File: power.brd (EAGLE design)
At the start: 27.6 x 17.8 mm, 12 parts, among them IC1 UC27775, J2 USB-MINIB-TH-VERTICAL-5PIN, U1 MCP73831, U2 Tiny85-20-SMT, X1 Micro USB

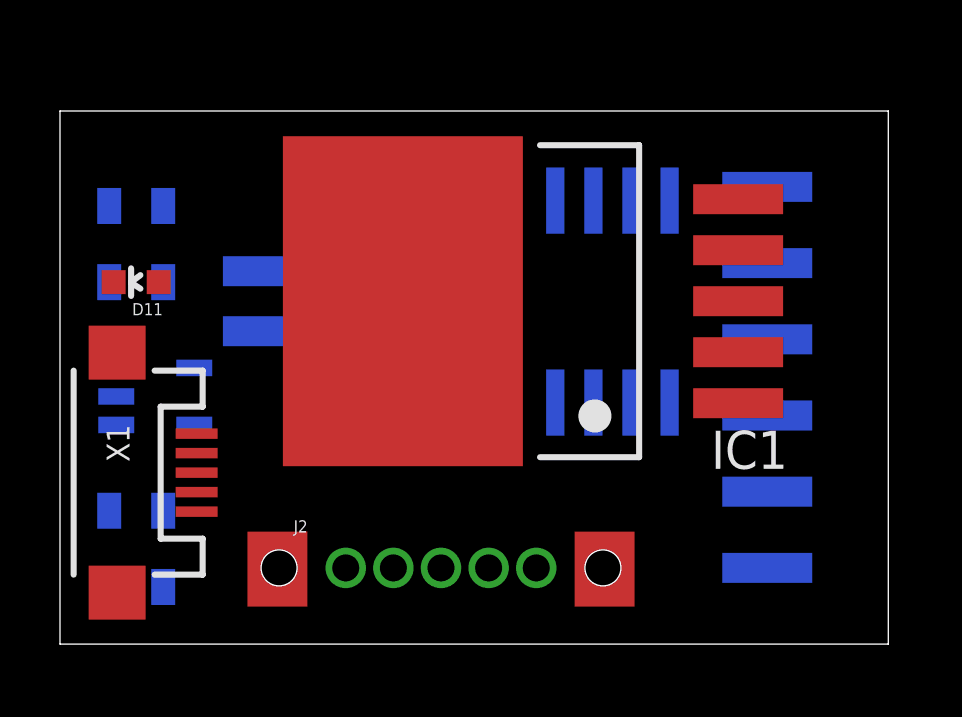
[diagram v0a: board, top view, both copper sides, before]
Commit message: Got a good handle on the bt module so went ahead and ordered one
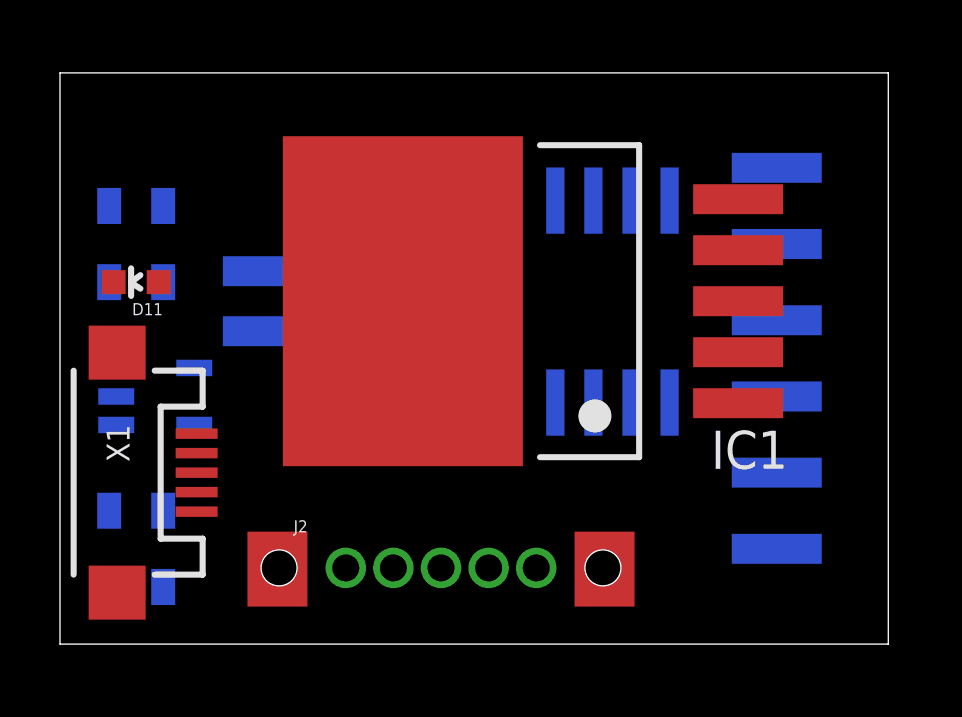
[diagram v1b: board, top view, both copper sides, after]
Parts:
- moved JP1 0.71 mm to (28.9, 9.53)
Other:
- board size 27.6 x 17.8 mm -> 27.6 x 19 mm
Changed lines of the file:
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@@
 <plain>
 <wire x1="0" y1="0" x2="27.61" y2="0" width="0" layer="20"/>
-<wire x1="27.61" y1="0" x2="27.61" y2="17.77" width="0" layer="20"/>
-<wire x1="27.61" y1="17.77" x2="0" y2="17.77" width="0" layer="20"/>
-<wire x1="0" y1="17.77" x2="0" y2="0" width="0" layer="20"/>
+<wire x1="27.61" y1="0" x2="27.61" y2="19.04" width="0" layer="20"/>
+<wire x1="27.61" y1="19.04" x2="0" y2="19.04" width="0" layer="20"/>
+<wire x1="0" y1="19.04" x2="0" y2="0" width="0" layer="20"/>
 <text x="8.89" y="23.495" size="1.778" layer="51">400mAh LiPo</text>
-<rectangle x1="29.845" y1="0" x2="59.055" y2="17.78" layer="52"/>
+<rectangle x1="29.845" y1="0" x2="59.3725" y2="19.05" layer="52"/>
 <text x="50.165" y="9.8425" size="1.016" layer="51" rot="R180">RN42-HID Module</text>
 <dimension x1="50.8" y1="0" x2="50.8" y2="33.5" x3="52.07" y3="16.75" textsize="1.016" layer="51"/>
@@
 <attribute name="PROD_ID" value="IC-09092" x="18.415" y="11.43" size="1.778" layer="28" rot="MR0" display="off"/>
 </element>
-<element name="JP1" library="mine" package="1X06-SMD-NOHOLES" value="RA 6Pin SMD" x="28.575" y="8.89" smashed="yes" rot="MR270">
-<attribute name="PROD_ID" value="CONN-08971" x="28.575" y="8.89" size="1.778" layer="28" rot="MR270" display="off"/>
-<attribute name="NAME" x="26.67" y="10.795" size="0.8128" layer="26" rot="MR270"/>
+<element name="JP1" library="mine" package="1X06-SMD-NOHOLES" value="RA 6Pin SMD" x="28.8925" y="9.525" smashed="yes" rot="MR270">
+<attribute name="PROD_ID" value="CONN-08971" x="28.8925" y="9.525" size="1.778" layer="28" rot="MR270" display="off"/>
+<attribute name="NAME" x="26.9875" y="11.43" size="0.8128" layer="26" rot="MR270"/>
 </element>
 <element name="IC1" library="mine" package="TO263_5" value="UC27775" x="14.605" y="11.43" rot="R90">
@@
 <contactref element="JP1" pad="6"/>
 <contactref element="IC1" pad="5"/>
-<wire x1="23.575" y1="2.54" x2="22.605" y2="14.83" width="0" layer="19" extent="1-16"/>
+<wire x1="23.8925" y1="3.175" x2="22.605" y2="14.83" width="0" layer="19" extent="1-16"/>
 <wire x1="7.73" y1="12.43" x2="22.605" y2="14.83" width="0" layer="19" extent="1-16"/>
 <wire x1="3.44" y1="14.605" x2="7.73" y2="12.43" width="0" layer="19" extent="16-16"/>
@@
 <contactref element="IC1" pad="3"/>
 <contactref element="J2" pad="GND"/>
-<wire x1="22.605" y1="11.43" x2="23.575" y2="15.24" width="0" layer="19" extent="1-16"/>
+<wire x1="22.605" y1="11.43" x2="23.8925" y2="15.875" width="0" layer="19" extent="1-16"/>
 <wire x1="7.73" y1="10.43" x2="22.605" y2="11.43" width="0" layer="19" extent="1-16"/>
 <wire x1="1.8749" y1="8.255" x2="7.73" y2="10.43" width="0" layer="19" extent="16-16"/>
@@
 <contactref element="JP1" pad="4"/>
 <contactref element="J2" pad="D-"/>
-<wire x1="11.1125" y1="2.54" x2="23.575" y2="7.62" width="0" layer="19" extent="16-16"/>
+<wire x1="11.1125" y1="2.54" x2="23.8925" y2="8.255" width="0" layer="19" extent="16-16"/>
 </signal>
 <signal name="N$3">
 <contactref element="JP1" pad="3"/>
 <contactref element="J2" pad="D+"/>
-<wire x1="12.7" y1="2.54" x2="23.575" y2="10.16" width="0" layer="19" extent="16-16"/>
+<wire x1="12.7" y1="2.54" x2="23.8925" y2="10.795" width="0" layer="19" extent="16-16"/>
 </signal>
 <signal name="VCC">
@@
 <contactref element="JP1" pad="5"/>
 <contactref element="J2" pad="VBUS"/>
-<wire x1="23.575" y1="5.08" x2="22.605" y2="13.13" width="0" layer="19" extent="1-16"/>
-<wire x1="9.525" y1="2.54" x2="23.575" y2="5.08" width="0" layer="19" extent="16-16"/>
+<wire x1="23.8925" y1="5.715" x2="22.605" y2="13.13" width="0" layer="19" extent="1-16"/>
+<wire x1="9.525" y1="2.54" x2="23.8925" y2="5.715" width="0" layer="19" extent="16-16"/>
 </signal>
 </signals>

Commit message: Added a switch and playing around with the arrangement
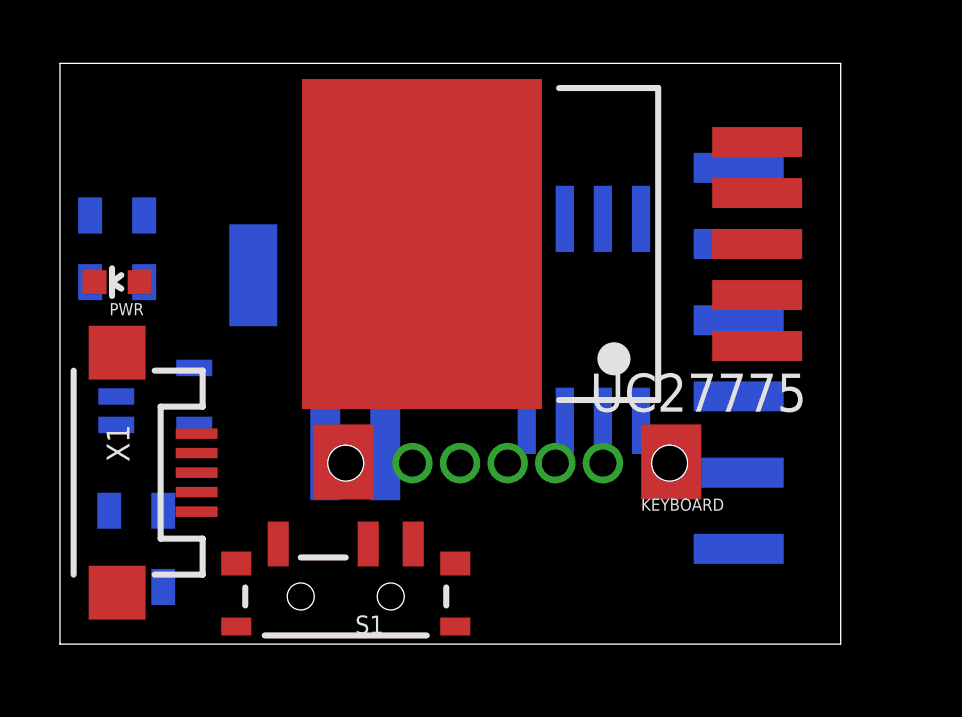
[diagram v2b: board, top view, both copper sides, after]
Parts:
- removed D11: RED, SparkFun:LED-0603
- removed IC1: UC27775, mine:TO263_5
- removed J2: USB-MINIB-TH-VERTICAL-5PIN, mine:USB-MINIB-TH-VERTICAL
- removed JP1: RA 6Pin SMD, mine:1X06-SMD-NOHOLES
- removed JP7: LiPo Battery, SparkFun:JST-2-SMD
- added BAT: LiPo Battery, SparkFun:JST-2-SMD
- added BT: RA 6Pin SMD, mine:1X06-SMD-NOHOLES
- added KEYBOARD: USB-MINIB-TH-VERTICAL-5PIN, mine:USB-MINIB-TH-VERTICAL
- added PWR: RED, SparkFun:LED-0603
- added S1: (no value), SparkFun-Electromechanical:SWITCH-SPST-SMD-A
- added UC27775: UC27775, mine:TO263_5
- moved U2 1.14 mm to (17.5, 10.8), turned to 180 degrees
- moved C2 0.71 mm to (1.91, 14.3)
- moved R1 0.64 mm to (1.91, 12.1), turned to 180 degrees
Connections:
- new net VBAT2: BAT.2, C2.1, S1.1, U1.3
- net GND: now also BAT.1, BT.1, KEYBOARD.GND, UC27775.3; no longer IC1.3, J2.GND, JP1.1, JP7.1
- net N$12: now also PWR.A; no longer D11.A
- net N$2: now also BT.4, KEYBOARD.D-; no longer J2.D-, JP1.4
- net N$3: now also BT.3, KEYBOARD.D+; no longer J2.D+, JP1.3
- net STAT: now also PWR.C; no longer D11.C
- net VBAT: now also BT.6, S1.3, UC27775.5; no longer C2.1, IC1.5, JP1.6, JP7.2, U1.3
- net VCC: now also BT.5, KEYBOARD.VBUS, UC27775.4; no longer IC1.4, J2.VBUS, JP1.5
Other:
- board size 27.6 x 19 mm -> 26 x 19.4 mm

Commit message: Using mini usb instead of micro
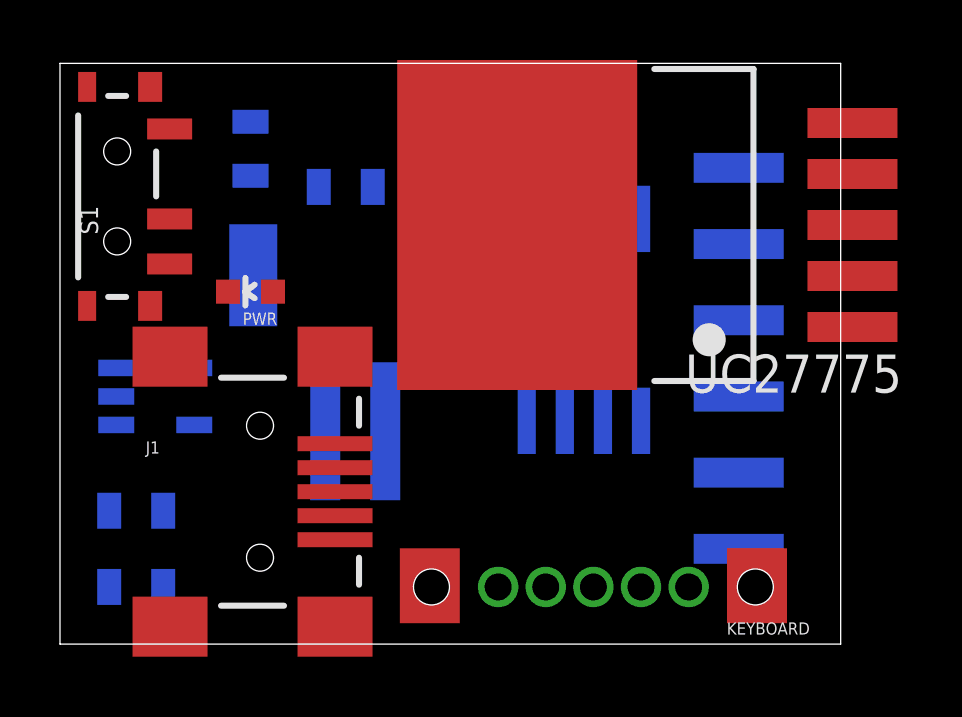
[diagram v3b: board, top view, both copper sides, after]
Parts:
- removed X1: Micro USB, SparkFun:USB-MICROB
- added J1: USB-MINIB-5PIN, SparkFun-Connectors:USB-MINIB
- moved S1 15.4 mm to (1.91, 14.9), turned to 90 degrees
- moved R1 8.25 mm to (9.53, 15.2)
- moved KEYBOARD 5.02 mm to (17.8, 1.91)
- moved C2 4.97 mm to (6.35, 16.5), turned to 270 degrees
- moved PWR 4.46 mm to (6.35, 11.7)
- moved UC27775 3.24 mm to (18.4, 14.0)
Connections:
- net GND: now also J1.GND; no longer X1.GND
- net VIN: now also J1.VBUS; no longer X1.VBUS
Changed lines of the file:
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@@
 <?xml version="1.0" encoding="utf-8"?>
 <!DOCTYPE eagle SYSTEM "eagle.dtd">
-<eagle version="6.6.0">
+<eagle version="7.4.0">
 <drawing>
 <settings>
@@
 <pass name="Default">
 <param name="RoutingGrid" value="50mil"/>
+<param name="AutoGrid" value="1"/>
+<param name="Efforts" value="0"/>
+<param name="TopRouterVariant" value="1"/>
 <param name="tpViaShape" value="round"/>
 <param name="PrefDir.1" value="|"/>
@@
 </autorouter>
 <elements>
-<element name="R1" library="SparkFun-Resistors" package="0805" value="330" x="1.905" y="12.065" rot="MR180">
-<attribute name="PROD_ID" value="RES-09883" x="1.905" y="12.065" size="1.778" layer="28" rot="MR180" display="off"/>
-</element>
-<element name="PWR" library="SparkFun" package="LED-0603" value="RED" x="1.905" y="12.065" rot="R90"/>
+<element name="R1" library="SparkFun-Resistors" package="0805" value="330" x="9.525" y="15.24" rot="MR180">
+<attribute name="PROD_ID" value="RES-09883" x="9.525" y="15.24" size="1.778" layer="28" rot="MR180" display="off"/>
+</element>
+<element name="PWR" library="SparkFun" package="LED-0603" value="RED" x="6.35" y="11.7475" rot="R90"/>
 <element name="U1" library="SparkFun" package="SOT23-5" value="MCP73831" x="3.175" y="8.255" rot="MR90"/>
 <element name="BAT" library="SparkFun" package="JST-2-SMD" value="LiPo Battery" x="9.8425" y="10.795" smashed="yes" rot="MR0">
@@
 <attribute name="VALUE" x="11.1125" y="10.795" size="0.4064" layer="28" rot="MR0"/>
 </element>
-<element name="X1" library="SparkFun" package="USB-MICROB" value="Micro USB" x="1.905" y="5.715" rot="R270"/>
 <element name="R2" library="SparkFun-Resistors" package="0805" value="2k" x="2.54" y="4.445" rot="MR180">
 <attribute name="PROD_ID" value="RES-09883" x="2.54" y="4.445" size="1.778" layer="28" rot="MR180" display="off"/>
@@
 <attribute name="PROD_ID" value="CAP-11625" x="2.54" y="1.905" size="1.778" layer="28" rot="MR0" display="off"/>
 </element>
-<element name="C2" library="SparkFun-Capacitors" package="0805-CAP" value="4.7uF" x="1.905" y="14.2875" rot="MR0">
-<attribute name="PROD_ID" value="CAP-11625" x="1.905" y="14.2875" size="1.778" layer="28" rot="MR0" display="off"/>
+<element name="C2" library="SparkFun-Capacitors" package="0805-CAP" value="4.7uF" x="6.35" y="16.51" rot="MR270">
+<attribute name="PROD_ID" value="CAP-11625" x="6.35" y="16.51" size="1.778" layer="28" rot="MR270" display="off"/>
 </element>
 <element name="U2" library="SparkFun-DigitalIC" package="SO08-EIAJ" value="Tiny85-20-SMT" x="17.4625" y="10.795" rot="MR180">
@@
 <attribute name="NAME" x="25.7175" y="11.43" size="0.8128" layer="26" rot="MR270"/>
 </element>
-<element name="UC27775" library="mine" package="TO263_5" value="UC27775" x="15.24" y="13.335" rot="R90">
-<attribute name="MF" value="TI" x="15.24" y="13.335" size="1.778" layer="27" rot="R90" display="off"/>
-</element>
-<element name="KEYBOARD" library="mine" package="USB-MINIB-TH-VERTICAL" value="USB-MINIB-TH-VERTICAL-5PIN" x="14.9225" y="6.0325" rot="R180">
-<attribute name="PROD_ID" value="CONN-08193" x="14.9225" y="6.0325" size="1.016" layer="27" rot="R180" display="off"/>
-</element>
-<element name="S1" library="SparkFun-Electromechanical" package="SWITCH-SPST-SMD-A" value="" x="9.525" y="1.5875" rot="R180"/>
+<element name="UC27775" library="mine" package="TO263_5" value="UC27775" x="18.415" y="13.97" rot="R90">
+<attribute name="MF" value="TI" x="18.415" y="13.97" size="1.778" layer="27" rot="R90" display="off"/>
+</element>
+<element name="KEYBOARD" library="mine" package="USB-MINIB-TH-VERTICAL" value="USB-MINIB-TH-VERTICAL-5PIN" x="17.78" y="1.905" rot="R180">
+<attribute name="PROD_ID" value="CONN-08193" x="17.78" y="1.905" size="1.016" layer="27" rot="R180" display="off"/>
+</element>
+<element name="S1" library="SparkFun-Electromechanical" package="SWITCH-SPST-SMD-A" value="" x="1.905" y="14.9225" rot="R90"/>
+<element name="J1" library="SparkFun-Connectors" package="USB-MINIB" value="USB-MINIB-5PIN" x="6.6675" y="5.08">
+<attribute name="PROD_ID" value="CONN-08193" x="6.6675" y="5.08" size="1.778" layer="27" display="off"/>
+</element>
 </elements>
 <signals>
@@
 <contactref element="UC27775" pad="5"/>
 <contactref element="S1" pad="3"/>
-<wire x1="22.6225" y1="3.175" x2="23.24" y2="16.735" width="0" layer="19" extent="1-16"/>
-<wire x1="7.275" y1="3.3375" x2="23.24" y2="16.735" width="0" layer="19" extent="1-1"/>
+<wire x1="22.6225" y1="3.175" x2="26.415" y2="17.37" width="0" layer="19" extent="1-16"/>
+<wire x1="3.655" y1="17.1725" x2="26.415" y2="17.37" width="0" layer="19" extent="1-1"/>
 </signal>
 <signal name="VIN">
 <contactref element="U1" pad="4"/>
-<contactref element="X1" pad="VBUS"/>
 <contactref element="C1" pad="1"/>
 <contactref element="R1" pad="1"/>
-<wire x1="4.4751" y1="9.205" x2="1.005" y2="12.065" width="0" layer="19" extent="16-16"/>
-<wire x1="4.555" y1="7.015" x2="4.4751" y2="9.205" width="0" layer="19" extent="1-16"/>
-<wire x1="3.44" y1="1.905" x2="4.555" y2="7.015" width="0" layer="19" extent="1-16"/>
+<contactref element="J1" pad="VBUS"/>
+<wire x1="8.625" y1="15.24" x2="4.4751" y2="9.205" width="0" layer="19" extent="16-16"/>
+<wire x1="9.1675" y1="6.68" x2="8.625" y2="15.24" width="0" layer="19" extent="1-16"/>
+<wire x1="3.44" y1="1.905" x2="4.4751" y2="9.205" width="0" layer="19" extent="16-16"/>
 </signal>
 <signal name="GND">
-<contactref element="X1" pad="GND"/>
 <contactref element="R2" pad="1"/>
 <contactref element="BT" pad="1"/>
@@
 <contactref element="C2" pad="2"/>
 <contactref element="BAT" pad="1"/>
-<wire x1="23.24" y1="13.335" x2="22.6225" y2="15.875" width="0" layer="19" extent="1-16"/>
-<wire x1="10.8425" y1="7.095" x2="23.24" y2="13.335" width="0" layer="19" extent="1-16"/>
-<wire x1="11.7475" y1="6.0325" x2="10.8425" y2="7.095" width="0" layer="19" extent="16-16"/>
-<wire x1="4.555" y1="4.415" x2="10.8425" y2="7.095" width="0" layer="19" extent="1-16"/>
-<wire x1="1.64" y1="4.445" x2="4.555" y2="4.415" width="0" layer="19" extent="1-16"/>
+<contactref element="J1" pad="GND"/>
+<wire x1="26.415" y1="13.97" x2="22.6225" y2="15.875" width="0" layer="19" extent="1-16"/>
+<wire x1="14.605" y1="1.905" x2="26.415" y2="13.97" width="0" layer="19" extent="1-1"/>
+<wire x1="10.8425" y1="7.095" x2="14.605" y2="1.905" width="0" layer="19" extent="16-16"/>
+<wire x1="1.8749" y1="8.255" x2="10.8425" y2="7.095" width="0" layer="19" extent="16-16"/>
+<wire x1="1.64" y1="4.445" x2="1.8749" y2="8.255" width="0" layer="19" extent="16-16"/>
 <wire x1="1.64" y1="1.905" x2="1.64" y2="4.445" width="0" layer="19" extent="16-16"/>
-<wire x1="1.8749" y1="8.255" x2="1.64" y2="4.445" width="0" layer="19" extent="16-16"/>
-<wire x1="1.005" y1="14.2875" x2="1.8749" y2="8.255" width="0" layer="19" extent="16-16"/>
+<wire x1="9.1675" y1="3.48" x2="1.64" y2="1.905" width="0" layer="19" extent="1-16"/>
+<wire x1="6.35" y1="15.61" x2="1.8749" y2="8.255" width="0" layer="19" extent="16-16"/>
 </signal>
 <signal name="N$12">
 <contactref element="PWR" pad="A"/>
 <contactref element="R1" pad="2"/>
-<wire x1="2.655" y1="12.065" x2="2.805" y2="12.065" width="0" layer="19" extent="1-16"/>
+<wire x1="7.1" y1="11.7475" x2="10.425" y2="15.24" width="0" layer="19" extent="1-16"/>
 </signal>
 <signal name="PROG">
@@
 <contactref element="PWR" pad="C"/>
 <contactref element="U1" pad="1"/>
-<wire x1="1.8749" y1="7.305" x2="1.155" y2="12.065" width="0" layer="19" extent="1-16"/>
+<wire x1="1.8749" y1="7.305" x2="5.6" y2="11.7475" width="0" layer="19" extent="1-16"/>
 </signal>
 <signal name="N$2">
 <contactref element="BT" pad="4"/>
 <contactref element="KEYBOARD" pad="D-"/>
-<wire x1="16.51" y1="6.0325" x2="22.6225" y2="8.255" width="0" layer="19" extent="16-16"/>
+<wire x1="19.3675" y1="1.905" x2="22.6225" y2="8.255" width="0" layer="19" extent="16-16"/>
 </signal>
 <signal name="N$3">
 <contactref element="BT" pad="3"/>
 <contactref element="KEYBOARD" pad="D+"/>
-<wire x1="14.9225" y1="6.0325" x2="22.6225" y2="10.795" width="0" layer="19" extent="16-16"/>
+<wire x1="17.78" y1="1.905" x2="22.6225" y2="10.795" width="0" layer="19" extent="16-16"/>
 </signal>
 <signal name="VCC">
@@
 <contactref element="BT" pad="5"/>
 <contactref element="KEYBOARD" pad="VBUS"/>
-<wire x1="22.6225" y1="5.715" x2="23.24" y2="15.035" width="0" layer="19" extent="1-16"/>
-<wire x1="18.0975" y1="6.0325" x2="22.6225" y2="5.715" width="0" layer="19" extent="16-16"/>
+<wire x1="22.6225" y1="5.715" x2="26.415" y2="15.67" width="0" layer="19" extent="1-16"/>
+<wire x1="20.955" y1="1.905" x2="22.6225" y2="5.715" width="0" layer="19" extent="16-16"/>
 </signal>
 <signal name="VBAT2">
@@
 <contactref element="BAT" pad="2"/>
 <contactref element="S1" pad="1"/>
-<wire x1="11.775" y1="3.3375" x2="2.805" y2="14.2875" width="0" layer="19" extent="1-16"/>
-<wire x1="1.8749" y1="9.205" x2="11.775" y2="3.3375" width="0" layer="19" extent="1-16"/>
+<wire x1="3.655" y1="12.6725" x2="6.35" y2="17.41" width="0" layer="19" extent="1-16"/>
+<wire x1="1.8749" y1="9.205" x2="3.655" y2="12.6725" width="0" layer="19" extent="1-16"/>
 <wire x1="8.8425" y1="7.095" x2="1.8749" y2="9.205" width="0" layer="19" extent="16-16"/>
 </signal>
